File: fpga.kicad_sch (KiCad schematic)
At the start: 65 parts, among them J14 Conn_01x06_Female, U14 TXU0304BQA

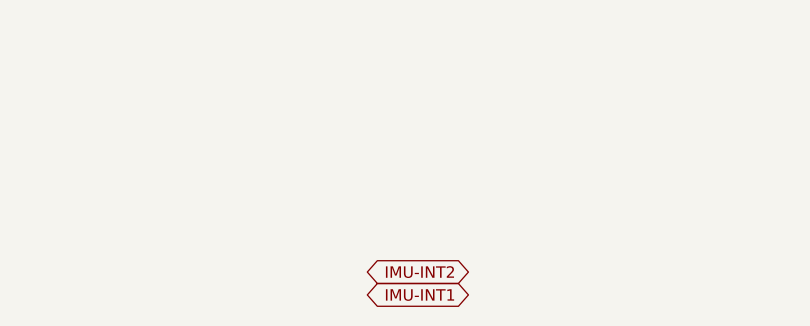
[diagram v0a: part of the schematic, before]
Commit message: Add CAN transceiver.  Clean up DRC warnings
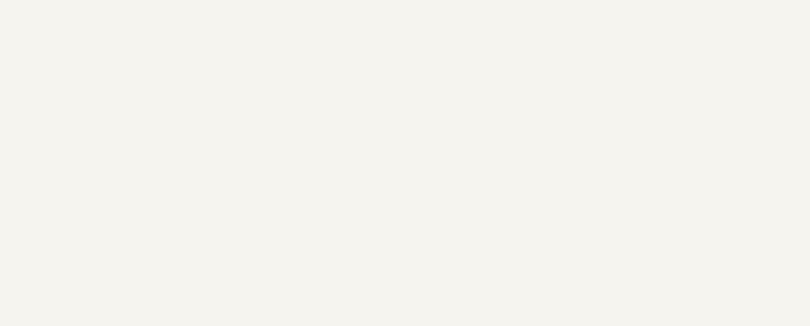
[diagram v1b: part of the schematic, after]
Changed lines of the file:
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@@
-    )
-  )
-  (global_label "IMU-INT1" (shape bidirectional) (at 118.5164 189.992 180) (fields_autoplaced)
-    (effects (font (size 1.27 1.27)) (justify right))
-    (property "Intersheet References" "${INTERSHEET_REFS}" (id 0) (at 107.1208 190.0714 0)
-      (effects (font (size 1.27 1.27)) (justify right) hide)
     )
   )
@@
       (effects (font (size 1.27 1.27)) (justify right) hide)
     )
-  )
-  (global_label "IMU-INT2" (shape bidirectional) (at 118.5164 187.452 180) (fields_autoplaced)
-    (effects (font (size 1.27 1.27)) (justify right))
-    (property "Intersheet References" "${INTERSHEET_REFS}" (id 0) (at 107.1208 187.5314 0)
-      (effects (font (size 1.27 1.27)) (justify right) hide)
-    )

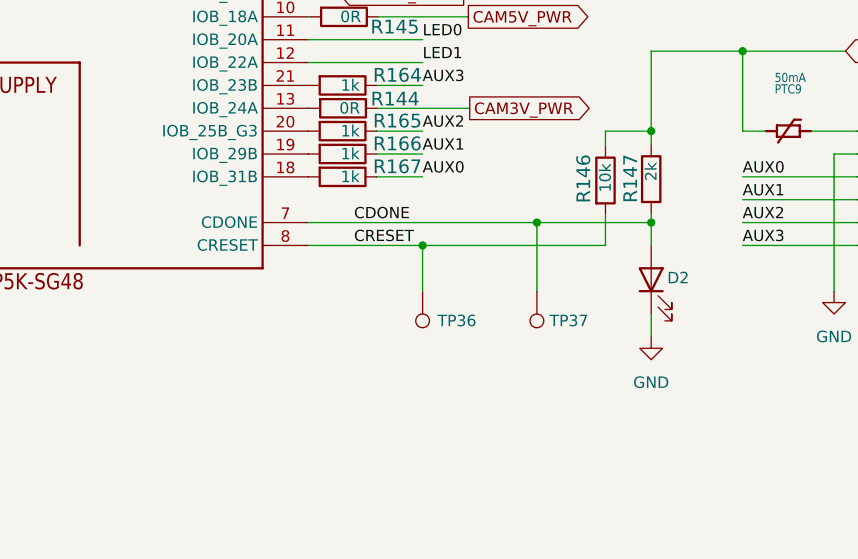
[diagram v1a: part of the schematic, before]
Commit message: Connect FPGA reset to host GPIO
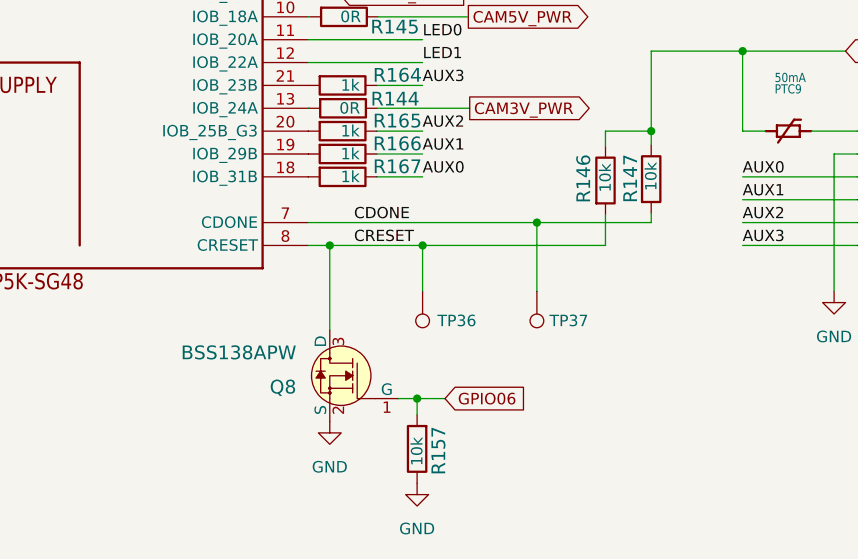
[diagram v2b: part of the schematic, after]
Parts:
- removed D2: LED, LED_SMD:LED_0603_1608Metric, symbol Device:LED
- added Q8: BSS138APW, jetson-nano-baseboard-footprints:SC70-3, symbol jetson-nano-baseboard:BSS138APW
- added R157: R_10k_0402, Resistor_SMD:R_0402_1005Metric, symbol jetson-nano-baseboard:R_10k_0402
- R147: value R_2k_0402 -> R_10k_0402; Val 2k -> 10k
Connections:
- net CRESET: now also Q8.3 (D)
- net GND: now also Q8.2 (S), R157.1
- new net GPIO06: Q8.1 (G), R157.2
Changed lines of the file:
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@@
   (junction (at 58.9788 86.2584) (diameter 0) (color 0 0 0 0)
   )
+  (junction (at 124.3076 139.7) (diameter 0) (color 0 0 0 0)
+  )
   (junction (at 269.3924 51.054) (diameter 0) (color 0 0 0 0)
   )
@@
   (junction (at 134.62 139.7) (diameter 0) (color 0 0 0 0)
   )
+  (junction (at 134.0104 156.718) (diameter 0) (color 0 0 0 0)
+  )
   (junction (at 195.2244 52.07) (diameter 0) (color 0 0 0 0)
   )
@@
   )
   (junction (at 55.88 129.54) (diameter 0) (color 0 0 0 0)
-  )
-  (junction (at 160.02 137.16) (diameter 0) (color 0 0 0 0)
   )
   (junction (at 66.04 119.38) (diameter 0) (color 0 0 0 0)
@@
     (stroke (width 0) (type default) (color 0 0 0 0))
   )
+  (wire (pts (xy 137.1092 156.718) (xy 134.0104 156.718))
+    (stroke (width 0) (type default) (color 0 0 0 0))
+  )
   (wire (pts (xy 182.88 127) (xy 177.8 127))
     (stroke (width 0) (type default) (color 0 0 0 0))
@@
     (stroke (width 0) (type default) (color 0 0 0 0))
   )
+  (wire (pts (xy 134.0104 156.718) (xy 134.0104 158.496))
+    (stroke (width 0) (type default) (color 0 0 0 0))
+  )
   (wire (pts (xy 129.54 129.54) (xy 134.62 129.54))
     (stroke (width 0) (type default) (color 0 0 0 0))
@@
     (stroke (width 0) (type default) (color 0 0 0 0))
   )
-  (wire (pts (xy 160.02 147.32) (xy 160.02 149.86))
-    (stroke (width 0) (type default) (color 0 0 0 0))
-  )
   (wire (pts (xy 132.08 86.36) (xy 137.16 86.36))
     (stroke (width 0) (type default) (color 0 0 0 0))
@@
     (stroke (width 0) (type default) (color 0 0 0 0))
   )
-  (wire (pts (xy 134.62 139.7) (xy 121.92 139.7))
+  (wire (pts (xy 134.62 139.7) (xy 124.3076 139.7))
     (stroke (width 0) (type default) (color 0 0 0 0))
   )
@@
     (stroke (width 0) (type default) (color 0 0 0 0))
   )
+  (wire (pts (xy 134.0104 156.718) (xy 131.9276 156.718))
+    (stroke (width 0) (type default) (color 0 0 0 0))
+  )
   (wire (pts (xy 57.15 95.1484) (xy 60.6044 95.1484))
     (stroke (width 0) (type default) (color 0 0 0 0))
@@
     (stroke (width 0) (type default) (color 0 0 0 0))
   )
+  (wire (pts (xy 124.3076 139.7) (xy 121.92 139.7))
+    (stroke (width 0) (type default) (color 0 0 0 0))
+  )
   (wire (pts (xy 58.9788 86.2584) (xy 72.8472 86.2584))
     (stroke (width 0) (type default) (color 0 0 0 0))
@@
     (stroke (width 0) (type default) (color 0 0 0 0))
   )
+  (wire (pts (xy 124.3076 139.7) (xy 124.3076 149.098))
+    (stroke (width 0) (type default) (color 0 0 0 0))
+  )
   (wire (pts (xy 124.46 88.9) (xy 121.92 88.9))
     (stroke (width 0) (type default) (color 0 0 0 0))
@@
   )
   (wire (pts (xy 154.94 127) (xy 160.02 127))
-    (stroke (width 0) (type default) (color 0 0 0 0))
-  )
-  (wire (pts (xy 160.02 137.16) (xy 160.02 139.7))
     (stroke (width 0) (type default) (color 0 0 0 0))
   )
@@
     (property "Intersheet References" "${INTERSHEET_REFS}" (id 0) (at 243.3373 51.1334 0)
       (effects (font (size 1.27 1.27)) (justify right) hide)
+    )
+  )
+  (global_label "GPIO06" (shape input) (at 137.1092 156.718 0) (fields_autoplaced)
+    (effects (font (size 1.27 1.27)) (justify left))
+    (property "Intersheet References" "${INTERSHEET_REFS}" (id 0) (at 146.3277 156.6386 0)
+      (effects (font (size 1.27 1.27)) (justify left) hide)
     )
   )
@@
     (pin "9")
   )
+  (symbol (lib_id "power:GND") (at 124.3076 159.258 0) (unit 1)
+    (in_bom yes) (on_board yes) (fields_autoplaced)
+    (property "Reference" "#PWR018" (id 0) (at 124.3076 165.608 0)
+      (effects (font (size 1.27 1.27)) hide)
+    )
+    (property "Value" "GND" (id 1) (at 124.3076 164.338 0))
+    (property "Footprint" "" (id 2) (at 124.3076 159.258 0)
+      (effects (font (size 1.27 1.27)) hide)
+    )
+    (property "Datasheet" "" (id 3) (at 124.3076 159.258 0)
+      (effects (font (size 1.27 1.27)) hide)
+    )
+    (pin "1")
+  )
   (symbol (lib_id "power:GND") (at 153.67 58.42 0) (unit 1)
     (in_bom yes) (on_board yes)
@@
     (pin "1")
   )
+  (symbol (lib_id "jetson-nano-baseboard:R_10k_0402") (at 134.0104 162.306 90) (unit 1)
+    (in_bom yes) (on_board yes)
+    (property "Reference" "R157" (id 0) (at 136.4234 165.227 0)
+      (effects (font (size 1.524 1.524)) (justify left))
+    )
+    (property "Value" "R_10k_0402" (id 1) (at 137.8204 162.306 0)
+      (effects (font (size 1.524 1.524)) hide)
+    )
+    (property "Footprint" "Resistor_SMD:R_0402_1005Metric" (id 2) (at 128.9304 157.226 0)
+      (effects (font (size 1.524 1.524)) (justify left) hide)
+    )
+    (property "Datasheet" "" (id 3) (at 134.0104 162.306 0)
+      (effects (font (size 1.27 1.27)) hide)
+    )
+    (property "Val" "10k" (id 6) (at 134.0104 164.211 0)
+      (effects (font (size 1.27 1.27)) (justify left))
+    )
+    (pin "1")
+    (pin "2")
+  )
+  (symbol (lib_id "jetson-nano-baseboard:BSS138APW") (at 124.3076 154.178 0) (mirror y) (unit 1)
+    (in_bom yes) (on_board yes) (fields_autoplaced)
+    (property "Reference" "Q8" (id 0) (at 120.5992 155.448 0)
+      (effects (font (size 1.524 1.524)) (justify left))
+    )
+    (property "Value" "BSS138APW" (id 1) (at 120.5992 151.638 0)
+      (effects (font (size 1.524 1.524)) (justify left))
+    )
+    (property "Footprint" "jetson-nano-baseboard-footprints:SC70-3" (id 2) (at 119.2276 149.098 0)
+      (effects (font (size 1.524 1.524)) (justify left) hide)
+    )
+    (property "Datasheet" "" (id 3) (at 119.2276 146.558 0)
+      (effects (font (size 1.524 1.524)) (justify left) hide)
+    )
+    (property "MPN" "BSS138PW" (id 4) (at 119.2276 141.478 0)
+      (effects (font (size 1.524 1.524)) (justify left) hide)
+    )
+    (property "Manufacturer" "ON Semiconductor" (id 5) (at 119.2276 126.238 0)
+      (effects (font (size 1.524 1.524)) (justify left) hide)
+    )
+    (pin "1")
+    (pin "2")
+    (pin "3")
+  )
   (symbol (lib_id "Connector:TestPoint") (at 328.8284 48.514 0) (unit 1)
     (in_bom yes) (on_board yes) (fields_autoplaced)
@@
     (pin "1")
     (pin "2")
-  )
-  (symbol (lib_id "power:GND") (at 160.02 149.86 0) (unit 1)
-    (in_bom yes) (on_board yes) (fields_autoplaced)
-    (property "Reference" "#PWR0128" (id 0) (at 160.02 156.21 0)
-      (effects (font (size 1.27 1.27)) hide)
-    )
-    (property "Value" "GND" (id 1) (at 160.02 154.94 0))
-    (property "Footprint" "" (id 2) (at 160.02 149.86 0)
-      (effects (font (size 1.27 1.27)) hide)
-    )
-    (property "Datasheet" "" (id 3) (at 160.02 149.86 0)
-      (effects (font (size 1.27 1.27)) hide)
-    )
-    (pin "1")
   )
   (symbol (lib_id "Connector:TestPoint") (at 147.32 144.78 180) (unit 1)
@@
     (pin "2")
   )
-  (symbol (lib_id "Device:LED") (at 160.02 143.51 90) (unit 1)
-    (in_bom yes) (on_board yes)
-    (property "Reference" "D2" (id 0) (at 161.798 143.3194 90)
-      (effects (font (size 1.27 1.27)) (justify right))
-    )
-    (property "Value" "LED" (id 1) (at 163.83 146.3674 90)
-      (effects (font (size 1.27 1.27)) (justify right) hide)
-    )
-    (property "Footprint" "LED_SMD:LED_0603_1608Metric" (id 2) (at 160.02 143.51 0)
-      (effects (font (size 1.27 1.27)) hide)
-    )
-    (property "Datasheet" "~" (id 3) (at 160.02 143.51 0)
-      (effects (font (size 1.27 1.27)) hide)
-    )
-    (pin "1")
-    (pin "2")
-  )
   (symbol (lib_id "power:GND") (at 146.05 105.41 0) (unit 1)
     (in_bom yes) (on_board yes)
@@
       (effects (font (size 1.524 1.524)) (justify left))
     )
-    (property "Value" "R_2k_0402" (id 1) (at 156.21 132.334 0)
+    (property "Value" "R_10k_0402" (id 1) (at 156.21 132.334 0)
       (effects (font (size 1.524 1.524)) hide)
     )
@@
       (effects (font (size 1.27 1.27)) hide)
     )
-    (property "Val" "2k" (id 6) (at 160.02 130.429 0)
+    (property "Val" "10k" (id 6) (at 160.02 130.429 0)
       (effects (font (size 1.27 1.27)) (justify left))
     )
@@
     (pin "2")
   )
+  (symbol (lib_id "power:GND") (at 134.0104 166.116 0) (unit 1)
+    (in_bom yes) (on_board yes) (fields_autoplaced)
+    (property "Reference" "#PWR019" (id 0) (at 134.0104 172.466 0)
+      (effects (font (size 1.27 1.27)) hide)
+    )
+    (property "Value" "GND" (id 1) (at 134.0104 171.196 0))
+    (property "Footprint" "" (id 2) (at 134.0104 166.116 0)
+      (effects (font (size 1.27 1.27)) hide)
+    )
+    (property "Datasheet" "" (id 3) (at 134.0104 166.116 0)
+      (effects (font (size 1.27 1.27)) hide)
+    )
+    (pin "1")
+  )
   (symbol (lib_id "jetson-nano-baseboard:C_100n_0402") (at 158.75 52.07 0) (mirror x) (unit 1)
